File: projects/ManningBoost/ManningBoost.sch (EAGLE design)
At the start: 27 parts, among them Q1 2N3904

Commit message: Final project updates. Ready to send to oshpark.
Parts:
- renumbered GND to G1, GND1 to G2, GND2 to G3, GND3 to G4, VIN to 9V
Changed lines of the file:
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@@
 <part name="CV" library="capacitors-elec" deviceset="063" device="1"/>
 <part name="CE" library="capacitors-elec" deviceset="063" device="1"/>
-<part name="GND" library="wirepad" deviceset="2,15/1,0" device=""/>
+<part name="G1" library="wirepad" deviceset="2,15/1,0" device=""/>
 <part name="IN" library="wirepad" deviceset="2,15/1,0" device=""/>
 <part name="BUF" library="wirepad" deviceset="2,15/1,0" device=""/>
 <part name="OUT" library="wirepad" deviceset="2,15/1,0" device=""/>
-<part name="VIN" library="wirepad" deviceset="2,15/1,0" device=""/>
+<part name="9V" library="wirepad" deviceset="2,15/1,0" device=""/>
 <part name="BOOST" library="potentiometers" deviceset="POTS" device=""/>
 <part name="VOL" library="potentiometers" deviceset="POTS" device="16MM"/>
 <part name="D2" library="diodes" deviceset="DO41" device=".2"/>
 <part name="CLIP" library="wirepad" deviceset="2,15/1,0" device=""/>
-<part name="GND1" library="wirepad" deviceset="2,15/1,0" device=""/>
-<part name="GND2" library="wirepad" deviceset="2,15/1,0" device=""/>
-<part name="GND3" library="wirepad" deviceset="2,15/1,0" device=""/>
+<part name="G2" library="wirepad" deviceset="2,15/1,0" device=""/>
+<part name="G3" library="wirepad" deviceset="2,15/1,0" device=""/>
+<part name="G4" library="wirepad" deviceset="2,15/1,0" device=""/>
 </parts>
 <sheets>
@@
 <instance part="CV" gate="G$1" x="55.88" y="86.36" rot="R180"/>
 <instance part="CE" gate="G$1" x="71.12" y="48.26" rot="R270"/>
-<instance part="GND" gate="1" x="48.26" y="33.02" rot="R90"/>
+<instance part="G1" gate="1" x="48.26" y="33.02" rot="R90"/>
 <instance part="IN" gate="1" x="30.48" y="58.42"/>
 <instance part="BUF" gate="1" x="73.66" y="53.34" rot="R180"/>
 <instance part="OUT" gate="1" x="99.06" y="55.88" rot="R180"/>
-<instance part="VIN" gate="1" x="63.5" y="93.98" rot="R270"/>
+<instance part="9V" gate="1" x="63.5" y="93.98" rot="R270"/>
 <instance part="BOOST" gate="G$1" x="71.12" y="40.64"/>
 <instance part="VOL" gate="G$1" x="91.44" y="55.88"/>
 <instance part="D2" gate="G$1" x="60.96" y="91.44"/>
 <instance part="CLIP" gate="1" x="93.98" y="63.5" rot="R180"/>
-<instance part="GND1" gate="1" x="53.34" y="33.02" rot="R90"/>
-<instance part="GND2" gate="1" x="63.5" y="33.02" rot="R90"/>
-<instance part="GND3" gate="1" x="71.12" y="33.02" rot="R90"/>
+<instance part="G2" gate="1" x="53.34" y="33.02" rot="R90"/>
+<instance part="G3" gate="1" x="63.5" y="33.02" rot="R90"/>
+<instance part="G4" gate="1" x="71.12" y="33.02" rot="R90"/>
 </instances>
 <busses>
@@
 <junction x="63.5" y="35.56"/>
 <pinref part="C2" gate="G$1" pin="2"/>
-<pinref part="GND" gate="1" pin="P"/>
+<pinref part="G1" gate="1" pin="P"/>
 <wire x1="48.26" y1="35.56" x2="48.26" y2="43.18" width="0.1524" layer="91"/>
 <wire x1="48.26" y1="35.56" x2="53.34" y2="35.56" width="0.1524" layer="91"/>
@@
 <wire x1="50.8" y1="86.36" x2="43.18" y2="86.36" width="0.1524" layer="91"/>
 <junction x="43.18" y="86.36"/>
-<pinref part="GND1" gate="1" pin="P"/>
-<pinref part="GND2" gate="1" pin="P"/>
-<pinref part="GND3" gate="1" pin="P"/>
+<pinref part="G2" gate="1" pin="P"/>
+<pinref part="G3" gate="1" pin="P"/>
+<pinref part="G4" gate="1" pin="P"/>
 </segment>
 </net>
@@
 <pinref part="RC" gate="G$1" pin="2"/>
 <pinref part="R1" gate="G$1" pin="1"/>
-<pinref part="VIN" gate="1" pin="P"/>
+<pinref part="9V" gate="1" pin="P"/>
 <junction x="63.5" y="91.44"/>
-<pinref part="VIN" gate="1" pin="P"/>
+<pinref part="9V" gate="1" pin="P"/>
 <pinref part="D2" gate="G$1" pin="C"/>
 <pinref part="CV" gate="G$1" pin="+"/>

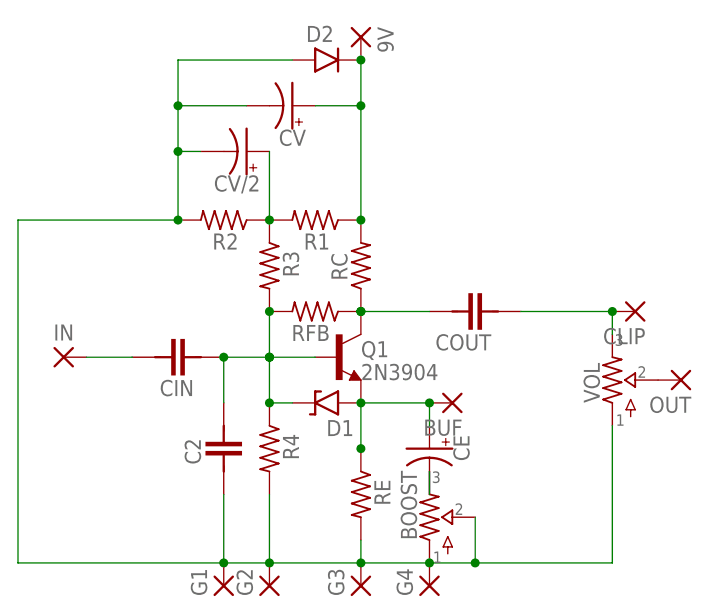
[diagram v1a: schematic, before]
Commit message: Updated to use new clipper block.
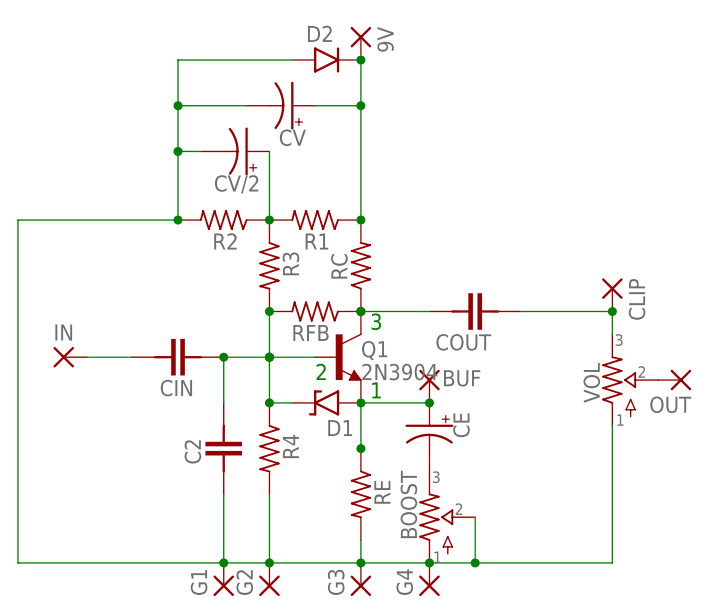
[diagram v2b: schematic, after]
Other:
- note added: "1"
- note added: "2"
- note added: "3"
- moved on the sheet: BUF, CE, CLIP
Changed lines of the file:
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@@
 <sheet>
 <plain>
+<text x="64.516" y="53.848" size="1.778" layer="91">1</text>
+<text x="58.42" y="55.88" size="1.778" layer="91">2</text>
+<text x="64.516" y="61.468" size="1.778" layer="91">3</text>
 </plain>
 <instances>
@@
 <instance part="CV/2" gate="G$1" x="50.8" y="81.28" rot="R180"/>
 <instance part="CV" gate="G$1" x="55.88" y="86.36" rot="R180"/>
-<instance part="CE" gate="G$1" x="71.12" y="48.26" rot="R270"/>
+<instance part="CE" gate="G$1" x="71.12" y="50.8" rot="R270"/>
 <instance part="G1" gate="1" x="48.26" y="33.02" rot="R90"/>
 <instance part="IN" gate="1" x="30.48" y="58.42"/>
-<instance part="BUF" gate="1" x="73.66" y="53.34" rot="R180"/>
+<instance part="BUF" gate="1" x="71.12" y="55.88" smashed="yes" rot="R270">
+<attribute name="NAME" x="72.517" y="55.1942" size="1.778" layer="95"/>
+<attribute name="VALUE" x="67.818" y="57.023" size="1.778" layer="96" rot="R270"/>
+</instance>
 <instance part="OUT" gate="1" x="99.06" y="55.88" rot="R180"/>
 <instance part="9V" gate="1" x="63.5" y="93.98" rot="R270"/>
@@
 <instance part="VOL" gate="G$1" x="91.44" y="55.88"/>
 <instance part="D2" gate="G$1" x="60.96" y="91.44"/>
-<instance part="CLIP" gate="1" x="93.98" y="63.5" rot="R180"/>
+<instance part="CLIP" gate="1" x="91.44" y="66.04" rot="R270"/>
 <instance part="G2" gate="1" x="53.34" y="33.02" rot="R90"/>
 <instance part="G3" gate="1" x="63.5" y="33.02" rot="R90"/>
@@
 <pinref part="CE" gate="G$1" pin="-"/>
 <pinref part="BOOST" gate="G$1" pin="3"/>
-<wire x1="71.12" y1="43.18" x2="71.12" y2="45.72" width="0.1524" layer="91"/>
 </segment>
 </net>
@@
 <pinref part="CE" gate="G$1" pin="+"/>
 <pinref part="BUF" gate="1" pin="P"/>
-<wire x1="71.12" y1="53.34" x2="71.12" y2="50.8" width="0.1524" layer="91"/>
 <pinref part="Q1" gate="G1" pin="E"/>
 <pinref part="D1" gate="G$1" pin="A"/>
